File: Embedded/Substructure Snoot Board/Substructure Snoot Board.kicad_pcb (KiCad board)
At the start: 2 copper layers, 28 parts, among them J1 D0 FFC, J2 D1 FFC, J3 L0 JST, J4 L1 JST, J5 XT30, U1 D0 FFC, U2 D1 FFC, U3 U FFC, U4 S FFC, U5 R FFC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

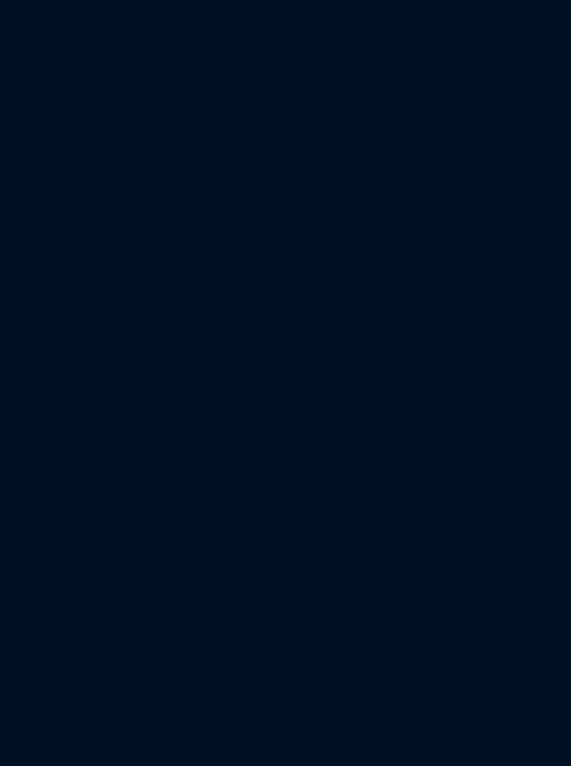
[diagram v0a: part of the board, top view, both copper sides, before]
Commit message: Added AOZ2264QI Symbol & Footprint
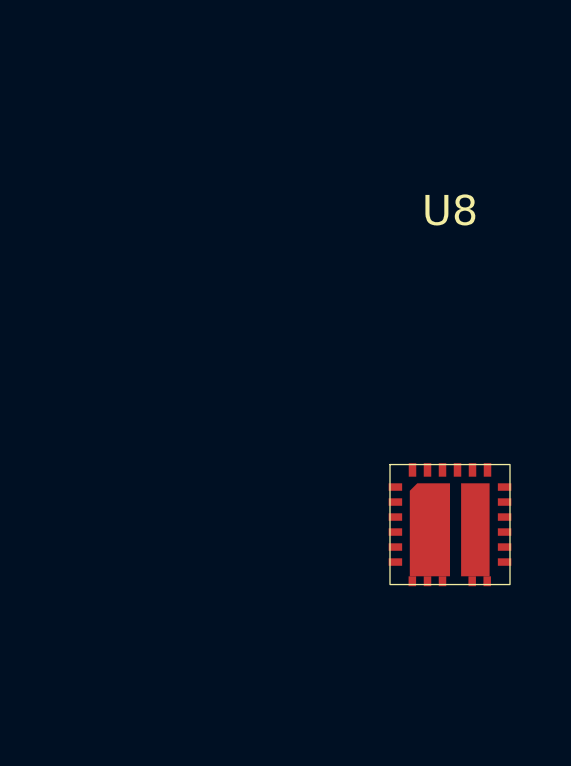
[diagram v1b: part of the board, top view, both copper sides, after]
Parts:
- added U8: ~, Power Regulator:AOZ2264QI, F.Cu at (141.3, 114.1)

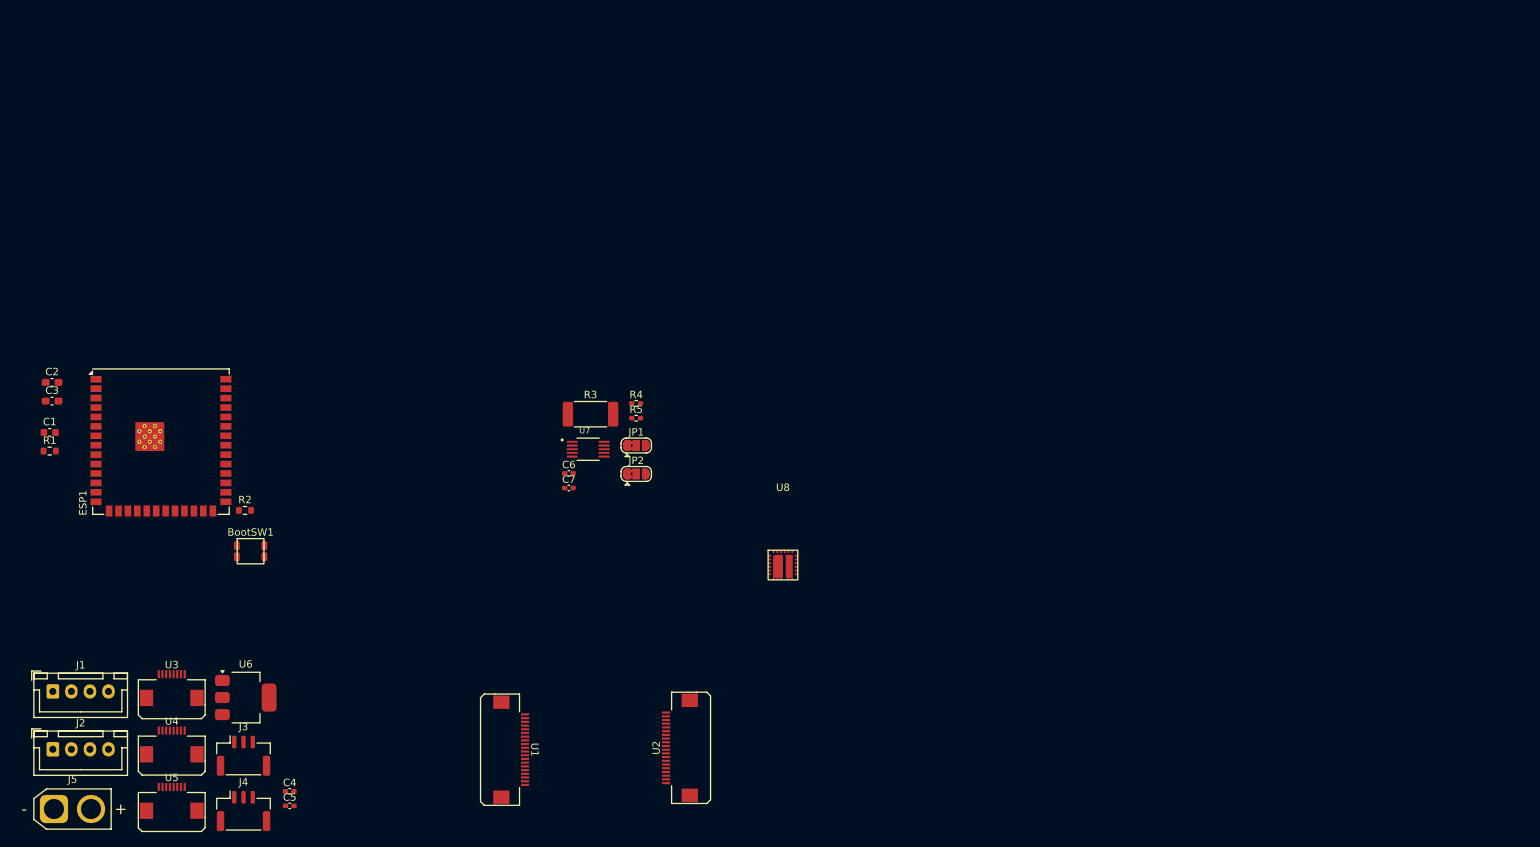
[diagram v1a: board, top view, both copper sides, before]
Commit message: Added Buck Converter PCB Basic Layout
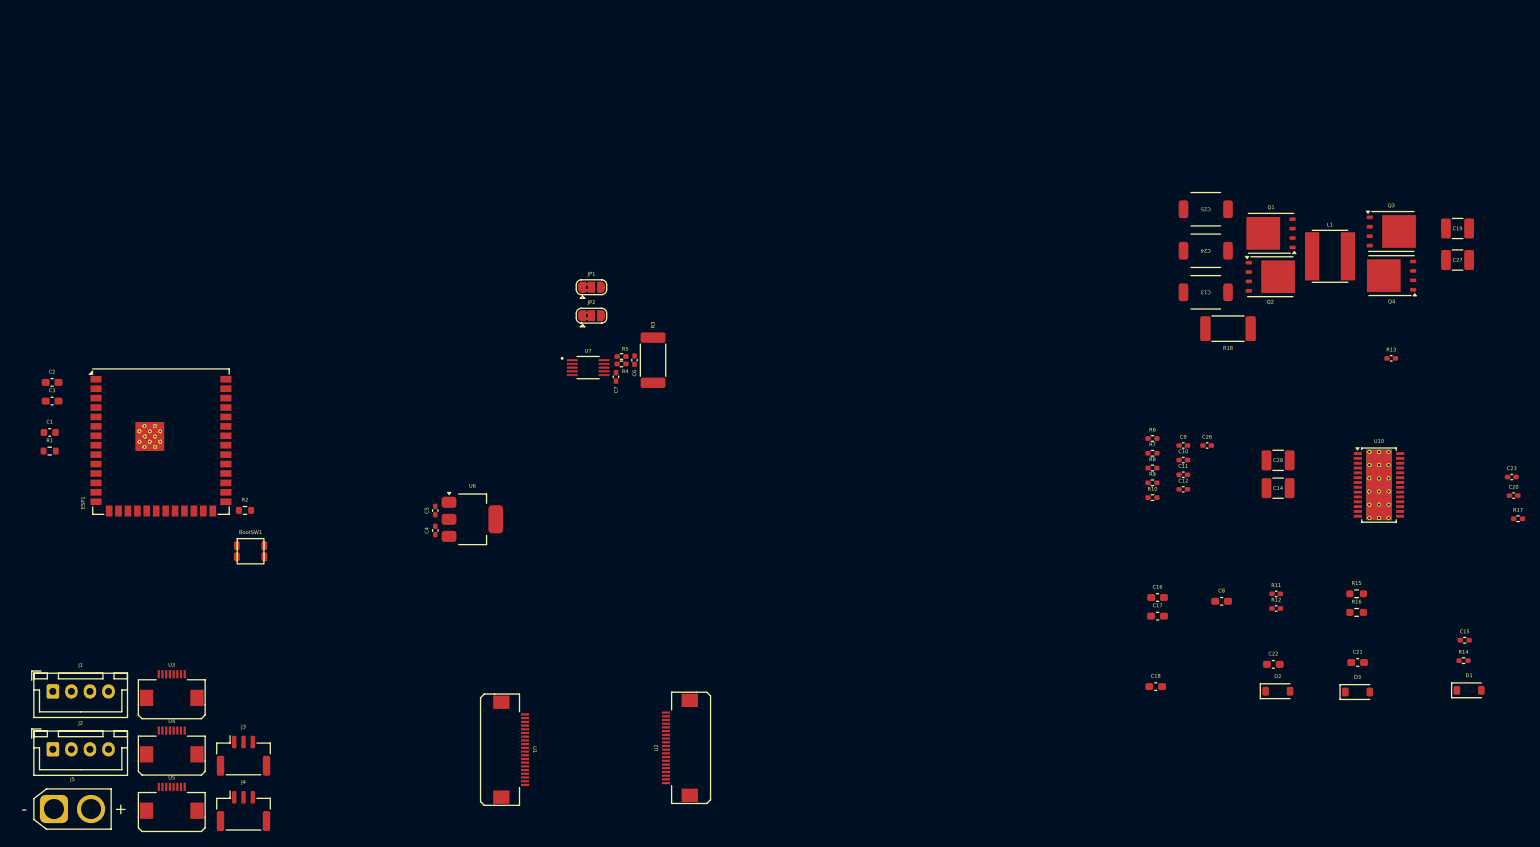
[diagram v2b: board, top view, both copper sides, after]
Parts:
- removed U8: ~, Power Regulator:AOZ2264QI
- added C10: 2nF 0ohm, Capacitor_SMD:C_0402_1005Metric_Pad0.74x0.62mm_HandSolder, F.Cu at (195.2, 100.0)
- added C11: 82pF 0ohm, Capacitor_SMD:C_0402_1005Metric_Pad0.74x0.62mm_HandSolder, F.Cu at (195.2, 101.9)
- added C12: 47pF 1mohms, Capacitor_SMD:C_0402_1005Metric_Pad0.74x0.62mm_HandSolder, F.Cu at (195.2, 103.9)
- added C13: 33uF 40mohm, Capacitors:EEFCX1E330R, F.Cu at (198.2, 77.3)
- added C14: 47uF 3mohm, Capacitor_SMD:C_1210_3225Metric_Pad1.33x2.70mm_HandSolder, F.Cu at (208.0, 103.8)
- added C15: 100nF 39mohm, Resistor_SMD:R_0402_1005Metric_Pad0.72x0.64mm_HandSolder, F.Cu at (233.2, 124.2)
- added C16: 22uF 3.71mohm, Capacitor_SMD:C_0603_1608Metric_Pad1.08x0.95mm_HandSolder, F.Cu at (191.8, 118.5)
- added C17: 22uF 3.71mohm, Capacitor_SMD:C_0603_1608Metric_Pad1.08x0.95mm_HandSolder, F.Cu at (191.8, 121.0)
- added C18: 22uF 3.71mohm, Capacitor_SMD:C_0603_1608Metric_Pad1.08x0.95mm_HandSolder, F.Cu at (191.5, 130.5)
- added C19: 47uF 3mohm, Capacitor_SMD:C_1210_3225Metric_Pad1.33x2.70mm_HandSolder, F.Cu at (232.2, 68.8)
- added C20: 1uF 11.4mohm, Capacitor_SMD:C_0402_1005Metric_Pad0.74x0.62mm_HandSolder, F.Cu at (239.8, 104.8)
- added C21: 100nF 50mohm, Capacitor_SMD:C_0603_1608Metric_Pad1.08x0.95mm_HandSolder, F.Cu at (218.7, 127.2)
- added C22: 100nF 50mohm, Capacitor_SMD:C_0603_1608Metric_Pad1.08x0.95mm_HandSolder, F.Cu at (207.4, 127.5)
- added C23: 100nF 1mohm, Capacitor_SMD:C_0402_1005Metric_Pad0.74x0.62mm_HandSolder, F.Cu at (239.5, 102.2)
- added C24: 33uF 40mohm, Capacitors:EEFCX1E330R, F.Cu at (198.2, 71.8)
- added C25: 33uF 40mohm, Capacitors:EEFCX1E330R, F.Cu at (198.2, 66.2)
- added C26: 6.8nF 523mohm, Capacitor_SMD:C_0402_1005Metric_Pad0.74x0.62mm_HandSolder, F.Cu at (198.4, 98.0)
- added C27: 47uF 3mohm, Capacitor_SMD:C_1210_3225Metric_Pad1.33x2.70mm_HandSolder, F.Cu at (232.2, 73.0)
- added C28: 47uF 3mohm, Capacitor_SMD:C_1210_3225Metric_Pad1.33x2.70mm_HandSolder, F.Cu at (208.0, 100.0)
- added C8: 12nF 0ohm, Capacitor_SMD:C_0603_1608Metric_Pad1.08x0.95mm_HandSolder, F.Cu at (200.4, 119.0)
- added C9: 6.8nF 523mohm, Capacitor_SMD:C_0402_1005Metric_Pad0.74x0.62mm_HandSolder, F.Cu at (195.2, 98.0)
- added D1: 385mV 500mA, Diode_SMD:D_SOD-123, F.Cu at (233.8, 131.0)
- added D2: 385mV 500mA, Diode_SMD:D_SOD-123, F.Cu at (208.0, 131.1)
- added D3: 385mV 500mA, Diode_SMD:D_SOD-123, F.Cu at (218.7, 131.2)
- added L1: 1uH 2.6mohm, Inductors:XAL7070-102ME, F.Cu at (215.0, 72.5)
- added Q1: CSD17577Q5A, Package_TO_SOT_SMD:TDSON-8-1, F.Cu at (207.1, 69.4)
- added Q2: CSD17577Q5A, Package_TO_SOT_SMD:TDSON-8-1, F.Cu at (206.9, 75.2)
- added Q3: CSD17573Q5B, Package_TO_SOT_SMD:TDSON-8-1, F.Cu at (223.2, 69.2)
- added Q4: CSD17577Q5A, Package_TO_SOT_SMD:TDSON-8-1, F.Cu at (223.3, 75.1)
- added R10: 100, Resistor_SMD:R_0402_1005Metric_Pad0.72x0.64mm_HandSolder, F.Cu at (191.1, 105.0)
- added R11: 249K, Capacitor_SMD:C_0402_1005Metric_Pad0.74x0.62mm_HandSolder, F.Cu at (207.8, 118.0)
- added R12: 110K, Capacitor_SMD:C_0402_1005Metric_Pad0.74x0.62mm_HandSolder, F.Cu at (207.8, 120.0)
- added R13: 2K, Capacitor_SMD:C_0402_1005Metric_Pad0.74x0.62mm_HandSolder, F.Cu at (223.2, 86.2)
- added R14: 10, Resistor_SMD:R_0402_1005Metric_Pad0.72x0.64mm_HandSolder, F.Cu at (233.0, 127.0)
- added R15: 105K, Resistor_SMD:R_0603_1608Metric_Pad0.98x0.95mm_HandSolder, F.Cu at (218.6, 118.0)
- added R16: 20K, Resistor_SMD:R_0603_1608Metric_Pad0.98x0.95mm_HandSolder, F.Cu at (218.6, 120.5)
- added R17: 10K, Resistor_SMD:R_0402_1005Metric_Pad0.72x0.64mm_HandSolder, F.Cu at (240.3, 107.9)
- added R18: 5m, Resistor_SMD:R_2512_6332Metric_Pad1.40x3.35mm_HandSolder, F.Cu at (201.2, 82.2)
- added R6: 732, Resistor_SMD:R_0402_1005Metric_Pad0.72x0.64mm_HandSolder, F.Cu at (191.1, 97.1)
- added R7: 93.1K, Resistor_SMD:R_0402_1005Metric_Pad0.72x0.64mm_HandSolder, F.Cu at (191.1, 99.0)
- added R8: 13K, Resistor_SMD:R_0402_1005Metric_Pad0.72x0.64mm_HandSolder, F.Cu at (191.1, 101.0)
- added R9: 100, Resistor_SMD:R_0402_1005Metric_Pad0.72x0.64mm_HandSolder, F.Cu at (191.1, 103.0)
- added U10: LM5176PWP, Package_SO:HTSSOP-28-1EP_4.4x9.7mm_P0.65mm_EP3.4x9.5mm_ThermalVias, F.Cu at (221.6, 103.3)
- moved C5 44.4 mm to (94.4, 106.8), turned to 90 degrees
- moved C4 40.3 mm to (94.4, 109.5), turned to 90 degrees
- moved U6 38.9 mm to (99.4, 108.0)
- moved JP1 22.2 mm to (115.5, 76.7)
- moved JP2 22.2 mm to (115.5, 80.5)
- moved C6 17.6 mm to (121.2, 86.5), turned to 90 degrees
- moved C7 16.3 mm to (118.8, 88.8), turned to 90 degrees
- moved R3 11.1 mm to (123.8, 86.5), turned to 90 degrees
- moved U7 11.0 mm to (115.0, 87.5)
- moved R5 8.55 mm to (119.5, 86.0), turned to 180 degrees
- moved R4 5.68 mm to (119.5, 87.0), turned to 180 degrees
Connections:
- C4 pad 1: +5VS -> +RAWVP
- J5 pad 2: +5VP -> +RAWVS
- R3 pad 1: +5VS -> +RAWVS
- R3 pad 2: +5VP -> +RAWVP
- R4 pad 1: +5VS -> +RAWVS
- R5 pad 1: +5VP -> +RAWVP
- U6 pad 3: +5VS -> +RAWVP

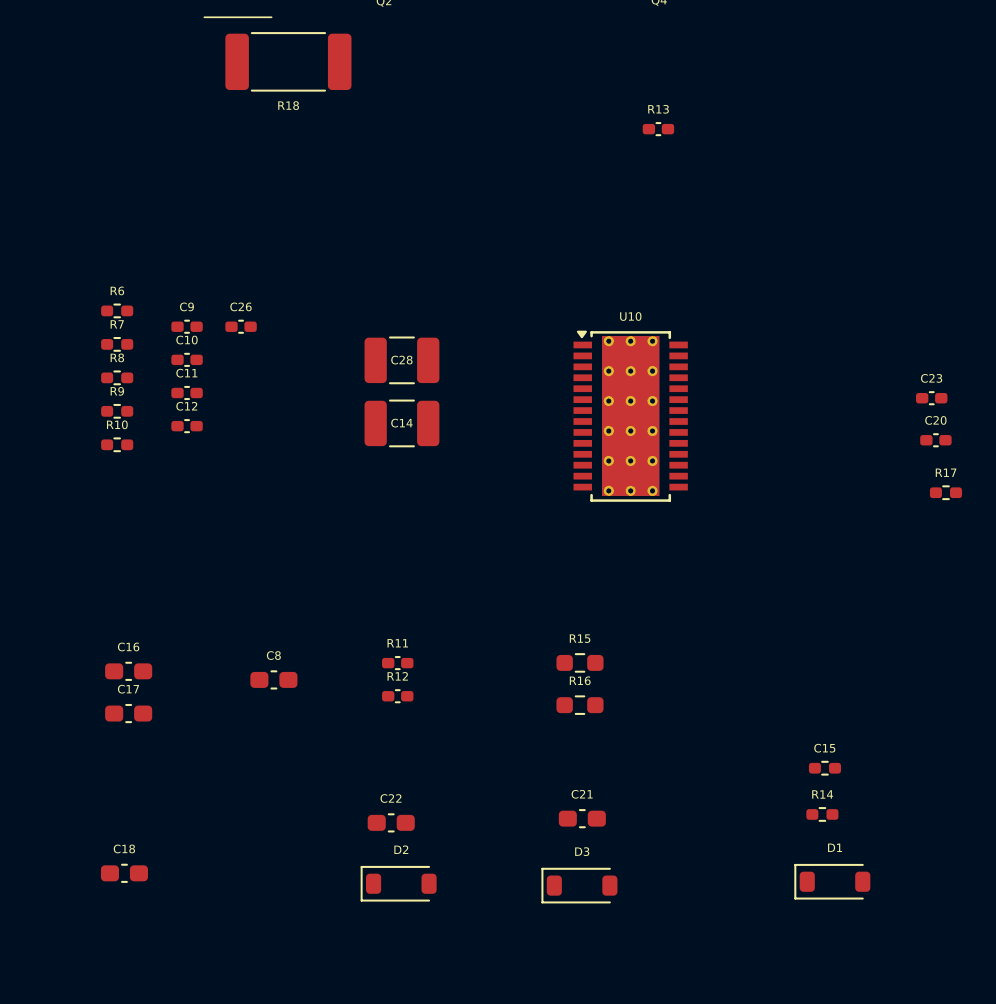
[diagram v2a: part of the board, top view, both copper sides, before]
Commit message: Added Buck Converter Essential Component Space Optimisation
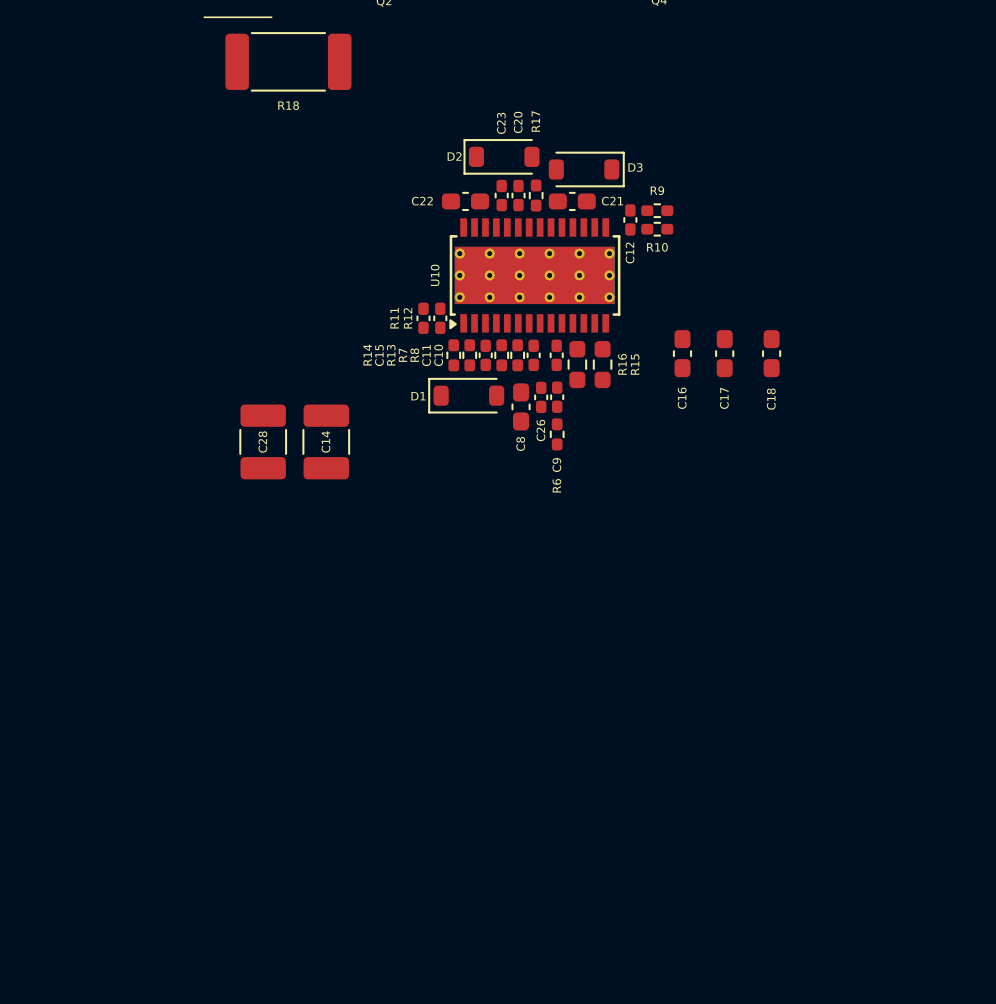
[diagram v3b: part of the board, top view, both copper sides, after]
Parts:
- moved C18 49.4 mm to (230.0, 99.6), turned to 90 degrees
- moved D2 43.7 mm to (214.1, 87.9)
- moved D3 42.6 mm to (218.8, 88.7), turned to 180 degrees
- moved C17 41.4 mm to (227.2, 99.6), turned to 90 degrees
- moved C16 38.0 mm to (224.7, 99.6), turned to 90 degrees
- moved C22 37.2 mm to (211.8, 90.5), turned to 180 degrees
- moved C21 36.7 mm to (218.1, 90.5)
- moved D1 36.2 mm to (212.0, 102.1)
- moved R14 35.0 mm to (211.1, 99.7), turned to 90 degrees
- moved R10 34.6 mm to (223.2, 92.2)
- moved R9 34.3 mm to (223.2, 91.1)
- moved C15 32.4 mm to (212.0, 99.7), turned to -90 degrees
- moved R17 30.1 mm to (216.0, 90.2), turned to 90 degrees
- moved C12 29.1 mm to (221.6, 91.7), turned to -90 degrees
- moved C20 28.8 mm to (214.9, 90.2), turned to 90 degrees
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
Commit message: Modified PCB from 2 Layers to 4 Layers
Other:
- copper layers 2 -> 4
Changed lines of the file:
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@@
 	(layers
 		(0 "F.Cu" signal)
+		(1 "In1.Cu" power)
+		(2 "In2.Cu" power)
 		(31 "B.Cu" signal)
 		(32 "B.Adhes" user "B.Adhesive")
@@
 	)
 	(setup
+		(stackup
+			(layer "F.SilkS"
+				(type "Top Silk Screen")
+			)
+			(layer "F.Paste"
+				(type "Top Solder Paste")
+			)
+			(layer "F.Mask"
+				(type "Top Solder Mask")
+				(thickness 0.01)
+			)
+			(layer "F.Cu"
+				(type "copper")
+				(thickness 0.035)
+			)
+			(layer "dielectric 1"
+				(type "prepreg")
+				(thickness 0.1)
+				(material "FR4")
+				(epsilon_r 4.5)
+				(loss_tangent 0.02)
+			)
+			(layer "In1.Cu"
+				(type "copper")
+				(thickness 0.035)
+			)
+			(layer "dielectric 2"
+				(type "core")
+				(thickness 1.24)
+				(material "FR4")
+				(epsilon_r 4.5)
+				(loss_tangent 0.02)
+			)
+			(layer "In2.Cu"
+				(type "copper")
+				(thickness 0.035)
+			)
+			(layer "dielectric 3"
+				(type "prepreg")
+				(thickness 0.1)
+				(material "FR4")
+				(epsilon_r 4.5)
+				(loss_tangent 0.02)
+			)
+			(layer "B.Cu"
+				(type "copper")
+				(thickness 0.035)
+			)
+			(layer "B.Mask"
+				(type "Bottom Solder Mask")
+				(thickness 0.01)
+			)
+			(layer "B.Paste"
+				(type "Bottom Solder Paste")
+			)
+			(layer "B.SilkS"
+				(type "Bottom Silk Screen")
+			)
+			(copper_finish "None")
+			(dielectric_constraints no)
+		)
 		(pad_to_mask_clearance 0)
 		(allow_soldermask_bridges_in_footprints no)
